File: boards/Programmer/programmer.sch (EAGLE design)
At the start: 2 parts

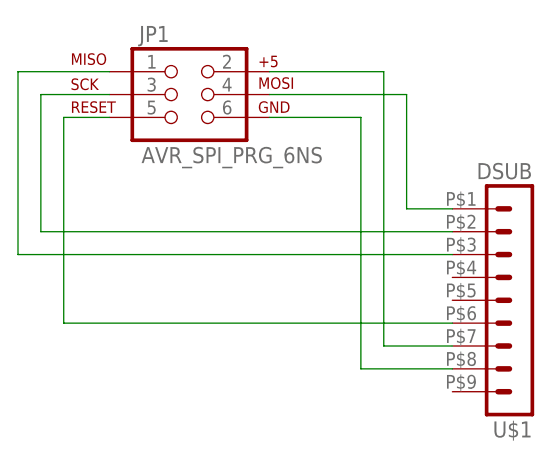
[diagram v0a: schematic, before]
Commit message: Updated programmer board to match BB2 Pinouts.
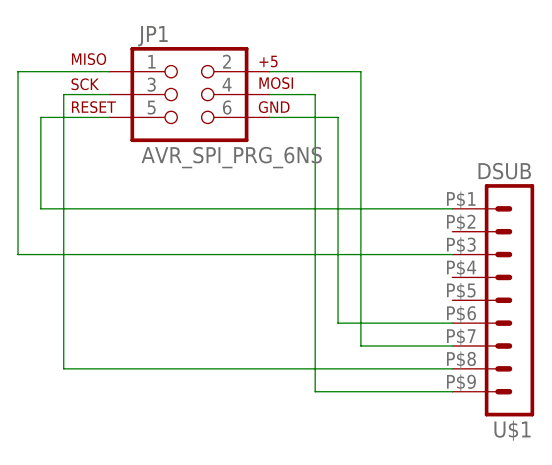
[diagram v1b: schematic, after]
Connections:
- net VDD renamed VCC
- net GND: now also U$1.6; no longer U$1.8
- net MOSI: now also U$1.9; no longer U$1.1
- net RESET: now also U$1.1; no longer U$1.6
- net SCK: now also U$1.8; no longer U$1.2
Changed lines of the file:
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@@
 </busses>
 <nets>
-<net name="VDD" class="0">
+<net name="RESET" class="0">
 <segment>
-<pinref part="JP1" gate="G$1" pin="2"/>
-<wire x1="71.12" y1="63.5" x2="83.82" y2="63.5" width="0.1524" layer="91"/>
-<wire x1="83.82" y1="63.5" x2="83.82" y2="33.02" width="0.1524" layer="91"/>
-<pinref part="U$1" gate="G$1" pin="7"/>
-<wire x1="83.82" y1="33.02" x2="91.44" y2="33.02" width="0.1524" layer="91"/>
-</segment>
-</net>
-<net name="GND" class="0">
-<segment>
-<pinref part="JP1" gate="G$1" pin="6"/>
-<wire x1="71.12" y1="58.42" x2="81.28" y2="58.42" width="0.1524" layer="91"/>
-<wire x1="81.28" y1="58.42" x2="81.28" y2="30.48" width="0.1524" layer="91"/>
-<pinref part="U$1" gate="G$1" pin="8"/>
-<wire x1="81.28" y1="30.48" x2="91.44" y2="30.48" width="0.1524" layer="91"/>
-</segment>
-</net>
-<net name="MOSI" class="0">
-<segment>
-<pinref part="JP1" gate="G$1" pin="4"/>
-<wire x1="71.12" y1="60.96" x2="86.36" y2="60.96" width="0.1524" layer="91"/>
-<wire x1="86.36" y1="60.96" x2="86.36" y2="48.26" width="0.1524" layer="91"/>
 <pinref part="U$1" gate="G$1" pin="1"/>
-<wire x1="86.36" y1="48.26" x2="91.44" y2="48.26" width="0.1524" layer="91"/>
+<wire x1="91.44" y1="48.26" x2="45.72" y2="48.26" width="0.1524" layer="91"/>
+<wire x1="45.72" y1="48.26" x2="45.72" y2="58.42" width="0.1524" layer="91"/>
+<pinref part="JP1" gate="G$1" pin="5"/>
+<wire x1="45.72" y1="58.42" x2="53.34" y2="58.42" width="0.1524" layer="91"/>
 </segment>
 </net>
@@
 </segment>
 </net>
+<net name="GND" class="0">
+<segment>
+<pinref part="U$1" gate="G$1" pin="6"/>
+<wire x1="91.44" y1="35.56" x2="78.74" y2="35.56" width="0.1524" layer="91"/>
+<wire x1="78.74" y1="35.56" x2="78.74" y2="58.42" width="0.1524" layer="91"/>
+<pinref part="JP1" gate="G$1" pin="6"/>
+<wire x1="78.74" y1="58.42" x2="71.12" y2="58.42" width="0.1524" layer="91"/>
+</segment>
+</net>
+<net name="VCC" class="0">
+<segment>
+<pinref part="U$1" gate="G$1" pin="7"/>
+<wire x1="91.44" y1="33.02" x2="81.28" y2="33.02" width="0.1524" layer="91"/>
+<wire x1="81.28" y1="33.02" x2="81.28" y2="63.5" width="0.1524" layer="91"/>
+<pinref part="JP1" gate="G$1" pin="2"/>
+<wire x1="81.28" y1="63.5" x2="71.12" y2="63.5" width="0.1524" layer="91"/>
+</segment>
+</net>
 <net name="SCK" class="0">
 <segment>
+<pinref part="U$1" gate="G$1" pin="8"/>
+<wire x1="91.44" y1="30.48" x2="48.26" y2="30.48" width="0.1524" layer="91"/>
+<wire x1="48.26" y1="30.48" x2="48.26" y2="60.96" width="0.1524" layer="91"/>
 <pinref part="JP1" gate="G$1" pin="3"/>
-<wire x1="53.34" y1="60.96" x2="45.72" y2="60.96" width="0.1524" layer="91"/>
-<wire x1="45.72" y1="60.96" x2="45.72" y2="45.72" width="0.1524" layer="91"/>
-<pinref part="U$1" gate="G$1" pin="2"/>
-<wire x1="45.72" y1="45.72" x2="91.44" y2="45.72" width="0.1524" layer="91"/>
+<wire x1="48.26" y1="60.96" x2="53.34" y2="60.96" width="0.1524" layer="91"/>
 </segment>
 </net>
-<net name="RESET" class="0">
+<net name="MOSI" class="0">
 <segment>
-<pinref part="JP1" gate="G$1" pin="5"/>
-<wire x1="53.34" y1="58.42" x2="48.26" y2="58.42" width="0.1524" layer="91"/>
-<wire x1="48.26" y1="58.42" x2="48.26" y2="35.56" width="0.1524" layer="91"/>
-<pinref part="U$1" gate="G$1" pin="6"/>
-<wire x1="48.26" y1="35.56" x2="91.44" y2="35.56" width="0.1524" layer="91"/>
+<pinref part="U$1" gate="G$1" pin="9"/>
+<wire x1="91.44" y1="27.94" x2="76.2" y2="27.94" width="0.1524" layer="91"/>
+<wire x1="76.2" y1="27.94" x2="76.2" y2="60.96" width="0.1524" layer="91"/>
+<pinref part="JP1" gate="G$1" pin="4"/>
+<wire x1="76.2" y1="60.96" x2="71.12" y2="60.96" width="0.1524" layer="91"/>
 </segment>
 </net>
